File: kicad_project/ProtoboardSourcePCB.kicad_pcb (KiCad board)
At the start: 2 copper layers, 53 x 62.9 mm, 10 parts, among them J1 Conn_02x05_Odd_Even, J2 Conn_02x05_Odd_Even

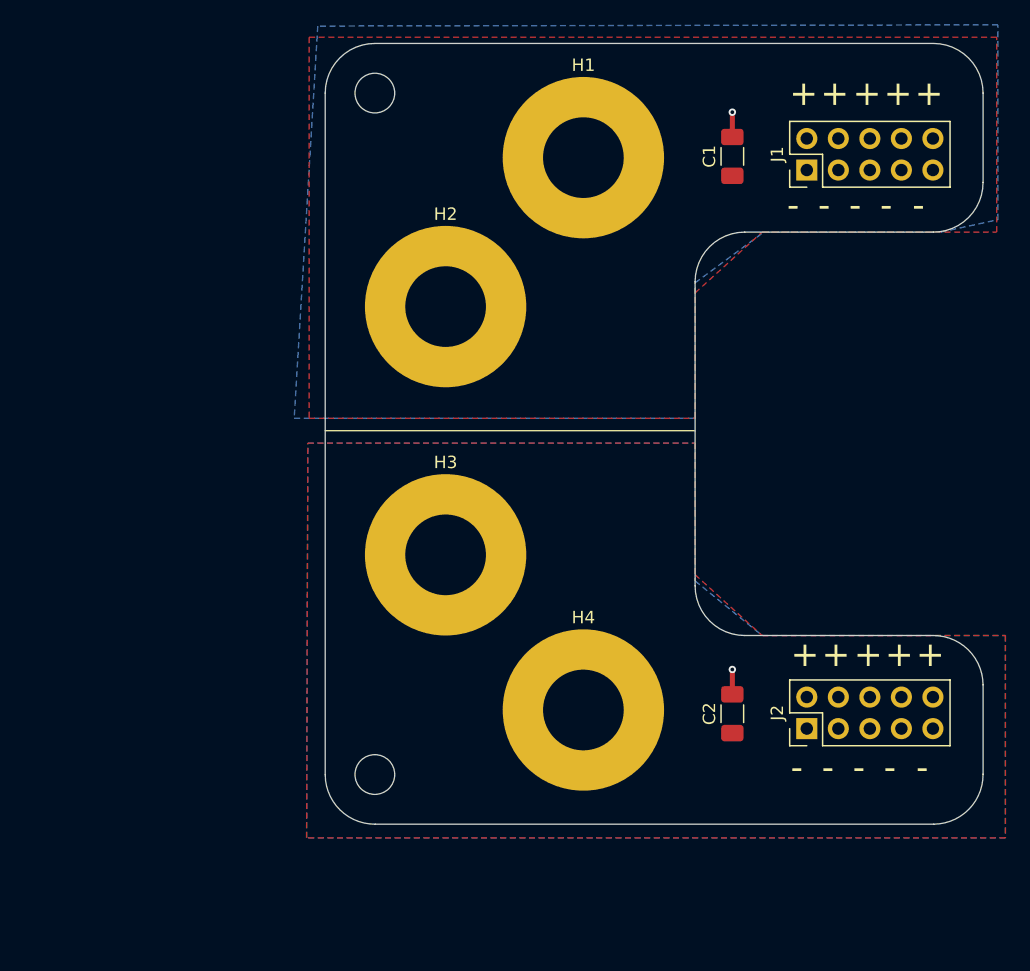
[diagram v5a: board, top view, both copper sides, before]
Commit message: Modificando huellas de conector banana y reacomodando huella de C2
Signed-off-by: RoMadrigal <rmadrigalmontes@gmail.com>
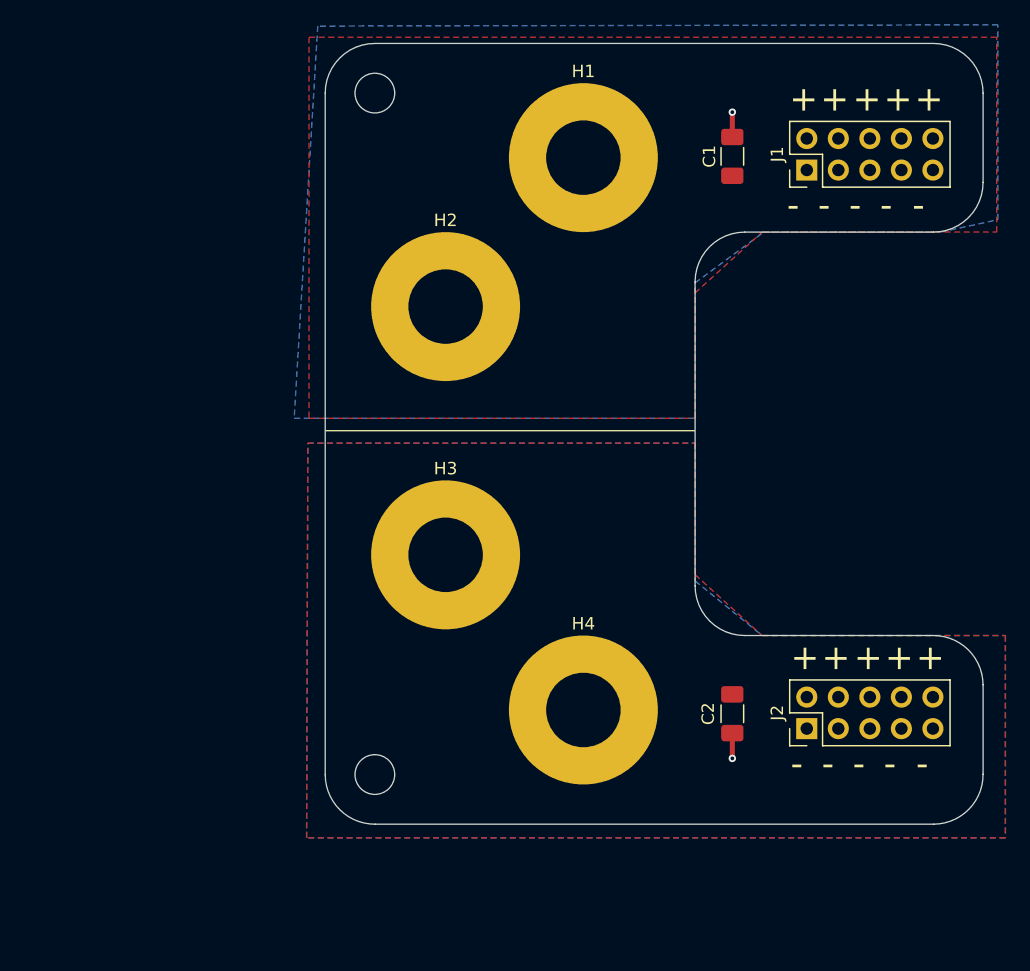
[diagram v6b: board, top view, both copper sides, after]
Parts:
- H1, H2, H3, H4: footprint MountingHole:MountingHole_6.5mm_Pad -> MountingHole:MountingHole_6mm_Pad
- turned C2 to -90 degrees

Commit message: Agregando especificaciones y nombres en la Silkscreen de la PCB
Signed-off-by: RoMadrigal <rmadrigalmontes@gmail.com>
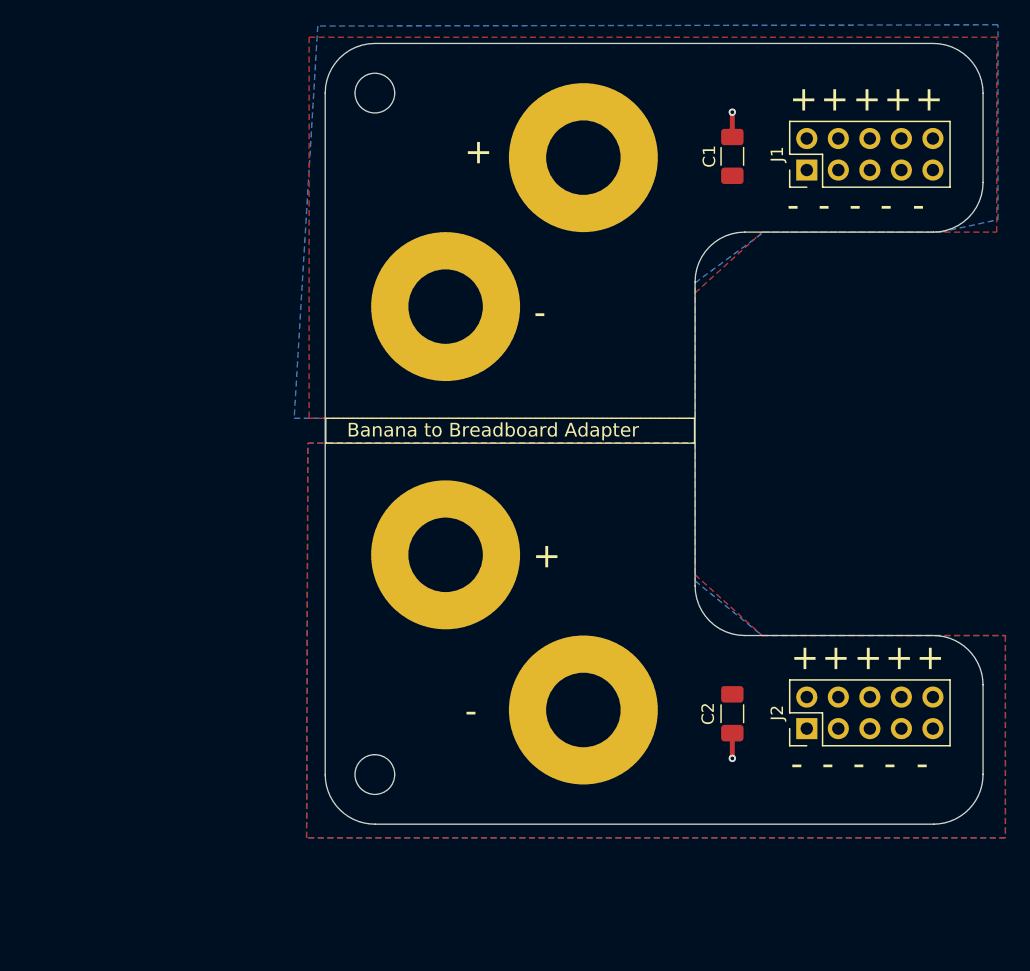
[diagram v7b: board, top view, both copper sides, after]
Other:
- board text added: "Banana to Breadboard Adapter"
- board text added: "Designed By: Rodrigo Madrigal Montes"
- board text added: "rmadrigalmontes@gmail.com"
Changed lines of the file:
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@@
 			(at 0 -6.95 0)
 			(layer "F.SilkS")
+			(hide yes)
 			(effects
 				(font
@@
 			(at 0 -6.95 0)
 			(layer "F.SilkS")
+			(hide yes)
 			(effects
 				(font
@@
 			(at 0 -6.95 0)
 			(layer "F.SilkS")
+			(hide yes)
 			(effects
 				(font
@@
 			(at 0 -6.95 0)
 			(layer "F.SilkS")
+			(hide yes)
 			(effects
 				(font
@@
 		(embedded_fonts no)
 	)
-	(gr_line
-		(start 110.25 71)
-		(end 139.95 71)
+	(gr_rect
+		(start 110.25 70)
+		(end 139.95 72)
 		(stroke
 			(width 0.1)
 			(type default)
 		)
+		(fill no)
 		(layer "F.SilkS")
 	)
@@
 		(start 109.7 70)
 		(end 140.8 70)
+		(stroke
+			(width 0.1)
+			(type default)
+		)
+		(layer "Dwgs.User")
+	)
+	(gr_line
+		(start 110.2 71)
+		(end 109.55 71)
+		(stroke
+			(width 0.1)
+			(type default)
+		)
+		(layer "Dwgs.User")
+	)
+	(gr_line
+		(start 140 71)
+		(end 140.9 71)
 		(stroke
 			(width 0.1)
@@
 			(font
 				(size 2 2)
-				(thickness 0.1)
+				(thickness 0.15)
 			)
 			(justify left bottom)
@@
 			(font
 				(size 2 2)
-				(thickness 0.1)
+				(thickness 0.15)
+			)
+			(justify left bottom)
+		)
+	)
+	(gr_text "Banana to Breadboard Adapter"
+		(at 111.95 71.6 0)
+		(layer "F.SilkS")
+		(effects
+			(font
+				(size 1.1 1.1)
+				(thickness 0.15)
 			)
 			(justify left bottom)
@@
 			(font
 				(size 2 2)
-				(thickness 0.1)
+				(thickness 0.15)
 			)
 			(justify left bottom)
@@
 			(font
 				(size 2 2)
-				(thickness 0.1)
+				(thickness 0.15)
 			)
 			(justify left bottom)
@@
 			(font
 				(size 2 2)
-				(thickness 0.1)
+				(thickness 0.15)
 			)
 			(justify left bottom)
@@
 			(font
 				(size 2 2)
-				(thickness 0.1)
+				(thickness 0.15)
 			)
 			(justify left bottom)
@@
 			(font
 				(size 2 2)
-				(thickness 0.1)
+				(thickness 0.15)
 			)
 			(justify left bottom)
@@
 			(font
 				(size 2 2)
-				(thickness 0.1)
+				(thickness 0.15)
 			)
 			(justify left bottom)
@@
 			(font
 				(size 2 2)
-				(thickness 0.1)
+				(thickness 0.15)
 			)
 			(justify left bottom)
@@
 			(font
 				(size 2 2)
-				(thickness 0.1)
+				(thickness 0.15)
 			)
 			(justify left bottom)
@@
 			(font
 				(size 2 2)
-				(thickness 0.1)
+				(thickness 0.15)
 			)
 			(justify left bottom)
@@
 			(font
 				(size 2 2)
-				(thickness 0.1)
+				(thickness 0.15)
 			)
 			(justify left bottom)
@@
 			(font
 				(size 2 2)
-				(thickness 0.1)
+				(thickness 0.15)
+			)
+			(justify left bottom)
+		)
+	)
+	(gr_text "+"
+		(at 121.4 49.7 0)
+		(layer "F.SilkS")
+		(effects
+			(font
+				(size 2 2)
+				(thickness 0.15)
+			)
+			(justify left bottom)
+		)
+	)
+	(gr_text "-"
+		(at 121.45 94.75 0)
+		(layer "F.SilkS")
+		(effects
+			(font
+				(size 2 2)
+				(thickness 0.15)
+			)
+			(justify left bottom)
+		)
+	)
+	(gr_text "-"
+		(at 127 62.65 0)
+		(layer "F.SilkS")
+		(effects
+			(font
+				(size 2 2)
+				(thickness 0.15)
 			)
 			(justify left bottom)
@@
 			(font
 				(size 2 2)
-				(thickness 0.1)
+				(thickness 0.15)
 			)
 			(justify left bottom)
@@
 			(font
 				(size 2 2)
-				(thickness 0.1)
+				(thickness 0.15)
 			)
 			(justify left bottom)
@@
 			(font
 				(size 2 2)
-				(thickness 0.1)
+				(thickness 0.15)
+			)
+			(justify left bottom)
+		)
+	)
+	(gr_text "+"
+		(at 126.9 82.25 0)
+		(layer "F.SilkS")
+		(effects
+			(font
+				(size 2 2)
+				(thickness 0.15)
 			)
 			(justify left bottom)
@@
 			(font
 				(size 2 2)
-				(thickness 0.1)
+				(thickness 0.15)
 			)
 			(justify left bottom)
@@
 			(font
 				(size 2 2)
-				(thickness 0.1)
+				(thickness 0.15)
 			)
 			(justify left bottom)
@@
 			(font
 				(size 2 2)
-				(thickness 0.1)
+				(thickness 0.15)
 			)
 			(justify left bottom)
@@
 			(font
 				(size 2 2)
-				(thickness 0.1)
-			)
-			(justify left bottom)
-		)
-	)
+				(thickness 0.15)
+			)
+			(justify left bottom)
+		)
+	)
+	(gr_text "Designed By: Rodrigo Madrigal Montes"
+		(at 136.2 86.15 270)
+		(layer "B.SilkS")
+		(effects
+			(font
+				(size 1 1)
+				(thickness 0.15)
+			)
+			(justify left bottom mirror)
+		)
+	)
+	(gr_text "rmadrigalmontes@gmail.com"
+		(at 133.1 82.35 270)
+		(layer "B.SilkS")
+		(effects
+			(font
+				(size 1 1)
+				(thickness 0.15)
+			)
+			(justify left bottom mirror)
+		)
+	)
